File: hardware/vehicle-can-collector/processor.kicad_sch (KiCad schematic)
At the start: 8 parts, among them SW201 SW_Push, U201 ATSAMC21J18A-AUT, U202 PL133-37TI, U203 ADM6320BX33ARJZ-R7, X201 ASV-12.000MHZ-EJ-T

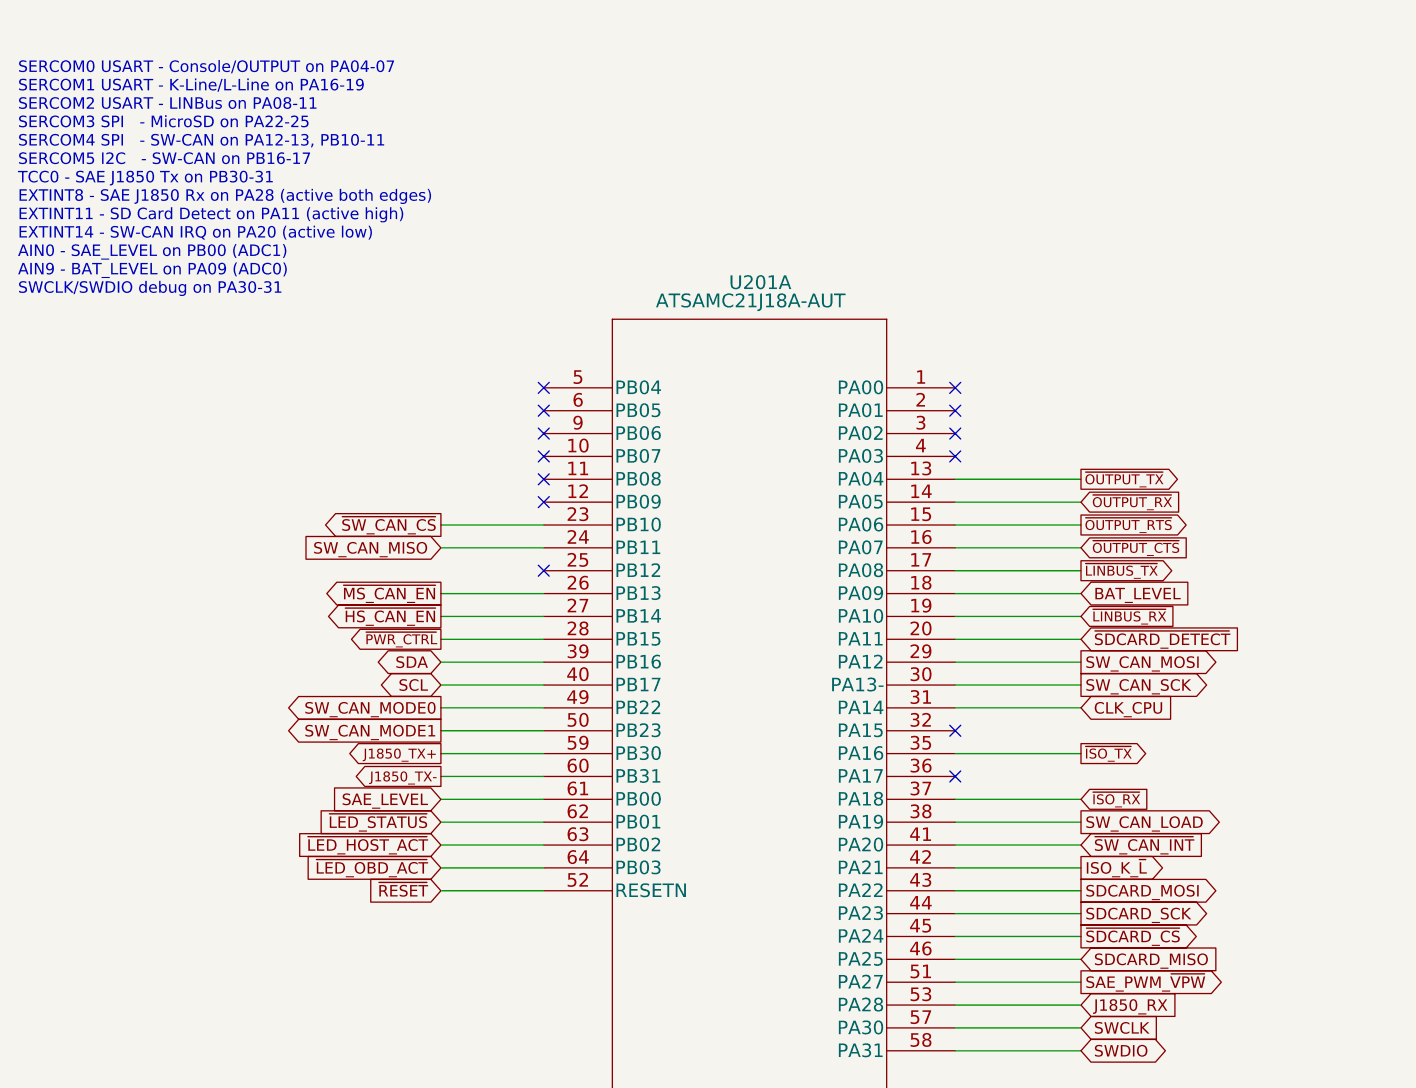
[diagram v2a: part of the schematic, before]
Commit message: Actually hook up CAN busses
- this required another pin shift.  DTS update to follow
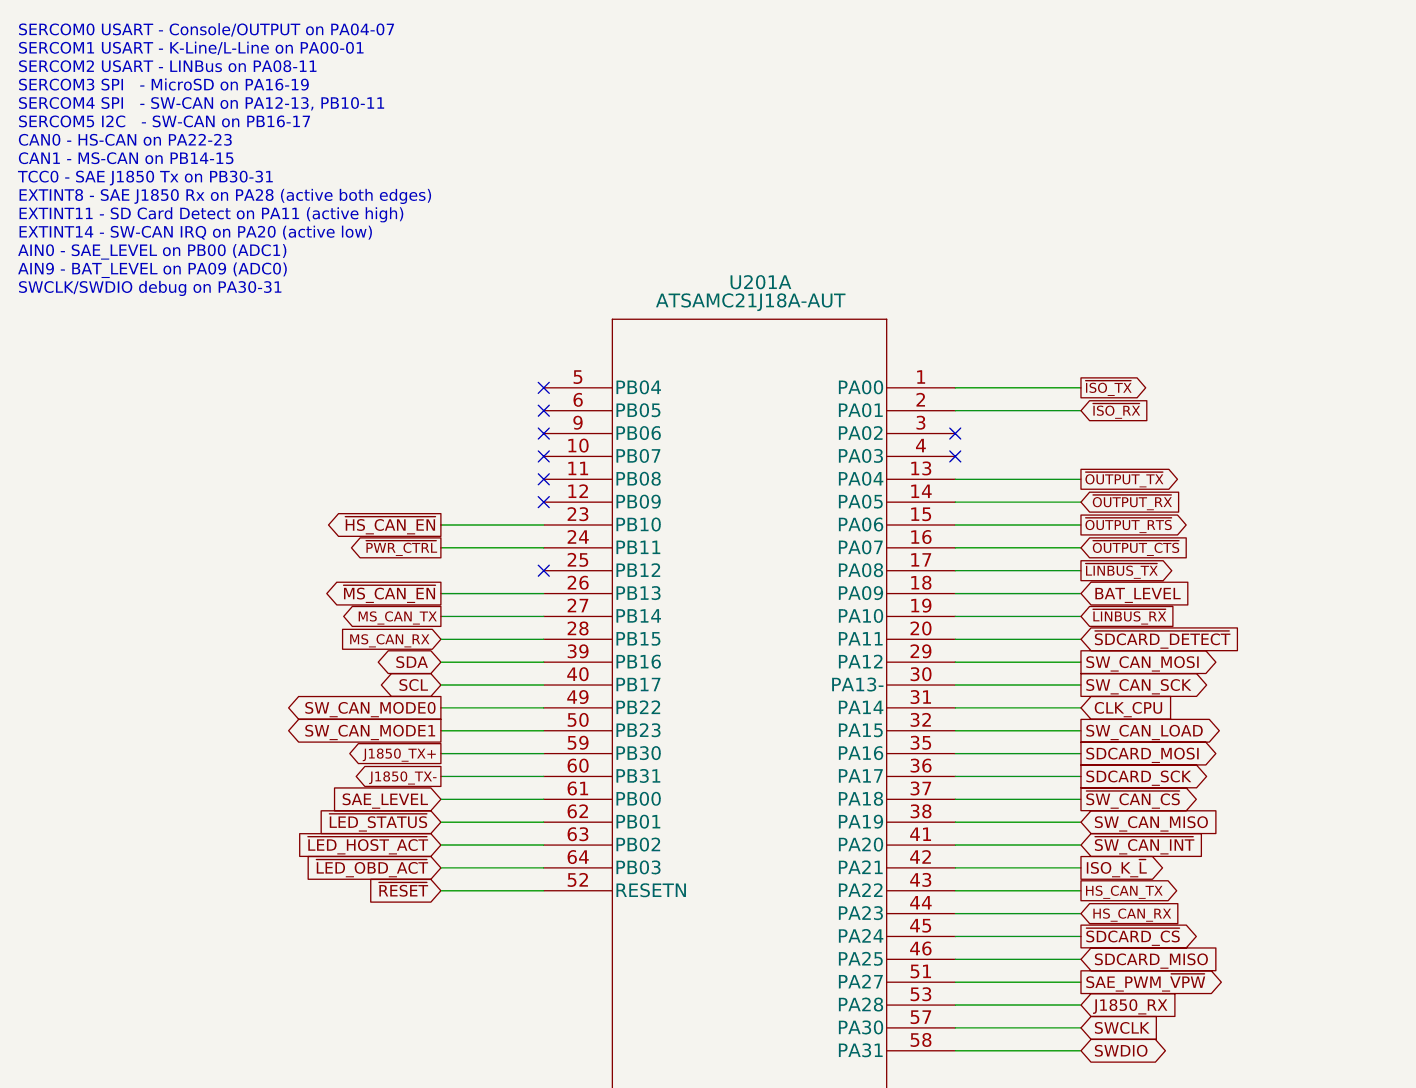
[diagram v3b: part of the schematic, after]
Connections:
- net SDCARD_MOSI: now also U201.35 (PA16); no longer U201.43 (PA22)
- net SDCARD_SCK: now also U201.36 (PA17); no longer U201.44 (PA23)
- net SW_CAN_LOAD: now also U201.32 (PA15); no longer U201.38 (PA19)
- net SW_CAN_MISO: now also U201.38 (PA19); no longer U201.24 (PB11)
- net ~{HS_CAN_EN}: now also U201.23 (PB10); no longer U201.27 (PB14)
- net ~{ISO_RX}: now also U201.2 (PA01); no longer U201.37 (PA18)
- net ~{ISO_TX}: now also U201.1 (PA00); no longer U201.35 (PA16)
- net ~{PWR_CTRL}: now also U201.24 (PB11); no longer U201.28 (PB15)
- net ~{SW_CAN_CS}: now also U201.37 (PA18); no longer U201.23 (PB10)
- new net HS_CAN_RX: U201.44 (PA23)
- new net HS_CAN_TX: U201.43 (PA22)
- new net MS_CAN_RX: U201.28 (PB15)
- new net MS_CAN_TX: U201.27 (PB14)
- no-connect marks 14 -> 10
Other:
- note added: "SERCOM0 USART - Console/OUTPUT on PA04-07 SERCOM1 USART - K-Line/L-Line on PA00-01 SERCOM2 USART - LINBus on PA08-11 SERCOM3 SPI - MicroSD on PA16-19 SERCOM4 SPI - SW-CAN on PA12-13, PB10-11 SERCOM5 I2C - SW-CAN on PB16-17 CAN0 - HS-CAN on PA22-23 CAN1 - MS-CAN on PB14-15 TCC0 - SAE J1850 Tx on PB30-31 EXTINT8 - SAE J1850 Rx on PA28 (active both edges) EXTINT11 - SD Card Detect on PA11 (active hi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"
- note removed: "SERCOM0 USART - Console/OUTPUT on PA04-07 SERCOM1 USART - K-Line/L-Line on PA16-19 SERCOM2 USART - LINBus on PA08-11 SERCOM3 SPI - MicroSD on PA22-25 SERCOM4 SPI - SW-CAN on PA12-13, PB10-11 SERCOM5 I2C - SW-CAN on PB16-17 TCC0 - SAE J1850 Tx on PB30-31 EXTINT8 - SAE J1850 Rx on PA28 (active both edges) EXTINT11 - SD Card Detect on PA11 (active high) EXTINT14 - SW-CAN IRQ on PA20 (active low) AIN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"

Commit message: Finished first round of layout.
- dang this has a lot of parts!
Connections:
- net HS_CAN_RX: now also U201.50 (PB23); no longer U201.44 (PA23)
- net HS_CAN_TX: now also U201.49 (PB22); no longer U201.43 (PA22)
- net SDCARD_MOSI: now also U201.43 (PA22); no longer U201.35 (PA16)
- net SDCARD_SCK: now also U201.44 (PA23); no longer U201.36 (PA17)
- net SW_CAN_LOAD: now also U201.36 (PA17); no longer U201.32 (PA15)
- net SW_CAN_MODE0: now also U201.5 (PB04); no longer U201.49 (PB22)
- net SW_CAN_MODE1: now also U201.6 (PB05); no longer U201.50 (PB23)
- net ~{HS_CAN_EN}: now also U201.25 (PB12); no longer U201.23 (PB10)
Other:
- note added: "SERCOM0 USART - Console/OUTPUT on PA04-07 SERCOM1 USART - K-Line/L-Line on PA00-01 SERCOM2 USART - LINBus on PA08-11 SERCOM3 SPI - MicroSD on PA22-25 SERCOM4 SPI - SW-CAN on PA12-13, PB10-11 SERCOM5 I2C - SW-CAN on PB16-17 CAN0 - HS-CAN on PB22-23 CAN1 - MS-CAN on PB14-15 TCC0 - SAE J1850 Tx on PB30-31 EXTINT8 - SAE J1850 Rx on PA28 (active both edges) EXTINT11 - SD Card Detect on PA11 (active hi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"
- note removed: "SERCOM0 USART - Console/OUTPUT on PA04-07 SERCOM1 USART - K-Line/L-Line on PA00-01 SERCOM2 USART - LINBus on PA08-11 SERCOM3 SPI - MicroSD on PA16-19 SERCOM4 SPI - SW-CAN on PA12-13, PB10-11 SERCOM5 I2C - SW-CAN on PB16-17 CAN0 - HS-CAN on PA22-23 CAN1 - MS-CAN on PB14-15 TCC0 - SAE J1850 Tx on PB30-31 EXTINT8 - SAE J1850 Rx on PA28 (active both edges) EXTINT11 - SD Card Detect on PA11 (active hi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"
